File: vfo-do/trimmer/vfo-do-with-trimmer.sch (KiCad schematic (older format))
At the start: 19 parts, among them J1 Fréquence, J10 GPS, J2 Bande, J3 Reset, J4 Résolution, J5 Si5351, J8 LCD, J9 Alim +12V, U1 L7805

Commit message: plaque standard 10x5
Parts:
- added TP1, TP2, TP3, TP4: TestPoint_Alt, MountingHole:MountingHole_3.2mm_M3_Pad_Via, symbol Connector:TestPoint_Alt
- A1: symbol arduino_nano_v3_5v_input:Arduino_Nano_v3.x -> vfo-do-with-trimmer-rescue:Arduino_Nano_v3.x-arduino_nano_v3_5v_input
- U1: symbol arduino_nano_v3_5v_input:L7805 -> vfo-do-with-trimmer-rescue:L7805-arduino_nano_v3_5v_input
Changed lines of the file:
@@
 	8450 1000 8700 1000
 $Comp
-L arduino_nano_v3_5v_input:Arduino_Nano_v3.x A1
+L vfo-do-with-trimmer-rescue:Arduino_Nano_v3.x-arduino_nano_v3_5v_input A1
 U 1 1 5F40DF5B
 P 1950 2050
@@
 Connection ~ 7600 1000
 $Comp
-L arduino_nano_v3_5v_input:L7805 U1
+L vfo-do-with-trimmer-rescue:L7805-arduino_nano_v3_5v_input U1
 U 1 1 5F44051C
 P 8150 1000
@@
 Text Label 9350 3950 0    50   ~ 0
 K
+$Comp
+L Connector:TestPoint_Alt TP1
+U 1 1 5F44EF81
+P 4800 1700
+F 0 "TP1" H 4858 1818 50  0000 L CNN
+F 1 "TestPoint_Alt" H 4858 1727 50  0000 L CNN
+F 2 "MountingHole:MountingHole_3.2mm_M3_Pad_Via" H 5000 1700 50  0001 C CNN
+F 3 "~" H 5000 1700 50  0001 C CNN
+	1    4800 1700
+	1    0    0    -1
+$EndComp
+$Comp
+L Connector:TestPoint_Alt TP2
+U 1 1 5F44F871
+P 5100 1700
+F 0 "TP2" H 5158 1818 50  0000 L CNN
+F 1 "TestPoint_Alt" H 5158 1727 50  0000 L CNN
+F 2 "MountingHole:MountingHole_3.2mm_M3_Pad_Via" H 5300 1700 50  0001 C CNN
+F 3 "~" H 5300 1700 50  0001 C CNN
+	1    5100 1700
+	1    0    0    -1
+$EndComp
+$Comp
+L Connector:TestPoint_Alt TP3
+U 1 1 5F44FBE5
+P 5450 1700
+F 0 "TP3" H 5508 1818 50  0000 L CNN
+F 1 "TestPoint_Alt" H 5508 1727 50  0000 L CNN
+F 2 "MountingHole:MountingHole_3.2mm_M3_Pad_Via" H 5650 1700 50  0001 C CNN
+F 3 "~" H 5650 1700 50  0001 C CNN
+	1    5450 1700
+	1    0    0    -1
+$EndComp
+$Comp
+L Connector:TestPoint_Alt TP4
+U 1 1 5F44FF88
+P 5750 1700
+F 0 "TP4" H 5808 1818 50  0000 L CNN
+F 1 "TestPoint_Alt" H 5808 1727 50  0000 L CNN
+F 2 "MountingHole:MountingHole_3.2mm_M3_Pad_Via" H 5950 1700 50  0001 C CNN
+F 3 "~" H 5950 1700 50  0001 C CNN
+	1    5750 1700
+	1    0    0    -1
+$EndComp
+$Comp
+L power:GND #PWR0124
+U 1 1 5F4502D5
+P 4800 1700
+F 0 "#PWR0124" H 4800 1450 50  0001 C CNN
+F 1 "GND" H 4805 1527 50  0000 C CNN
+F 2 "" H 4800 1700 50  0001 C CNN
+F 3 "" H 4800 1700 50  0001 C CNN
+	1    4800 1700
+	1    0    0    -1
+$EndComp
+$Comp
+L power:GND #PWR0125
+U 1 1 5F450BEC
+P 5100 1700
+F 0 "#PWR0125" H 5100 1450 50  0001 C CNN
+F 1 "GND" H 5105 1527 50  0000 C CNN
+F 2 "" H 5100 1700 50  0001 C CNN
+F 3 "" H 5100 1700 50  0001 C CNN
+	1    5100 1700
+	1    0    0    -1
+$EndComp
+$Comp
+L power:GND #PWR0126
+U 1 1 5F451044
+P 5450 1700
+F 0 "#PWR0126" H 5450 1450 50  0001 C CNN
+F 1 "GND" H 5455 1527 50  0000 C CNN
+F 2 "" H 5450 1700 50  0001 C CNN
+F 3 "" H 5450 1700 50  0001 C CNN
+	1    5450 1700
+	1    0    0    -1
+$EndComp
+$Comp
+L power:GND #PWR0127
+U 1 1 5F451422
+P 5750 1700
+F 0 "#PWR0127" H 5750 1450 50  0001 C CNN
+F 1 "GND" H 5755 1527 50  0000 C CNN
+F 2 "" H 5750 1700 50  0001 C CNN
+F 3 "" H 5750 1700 50  0001 C CNN
+	1    5750 1700
+	1    0    0    -1
+$EndComp
 $EndSCHEMATC

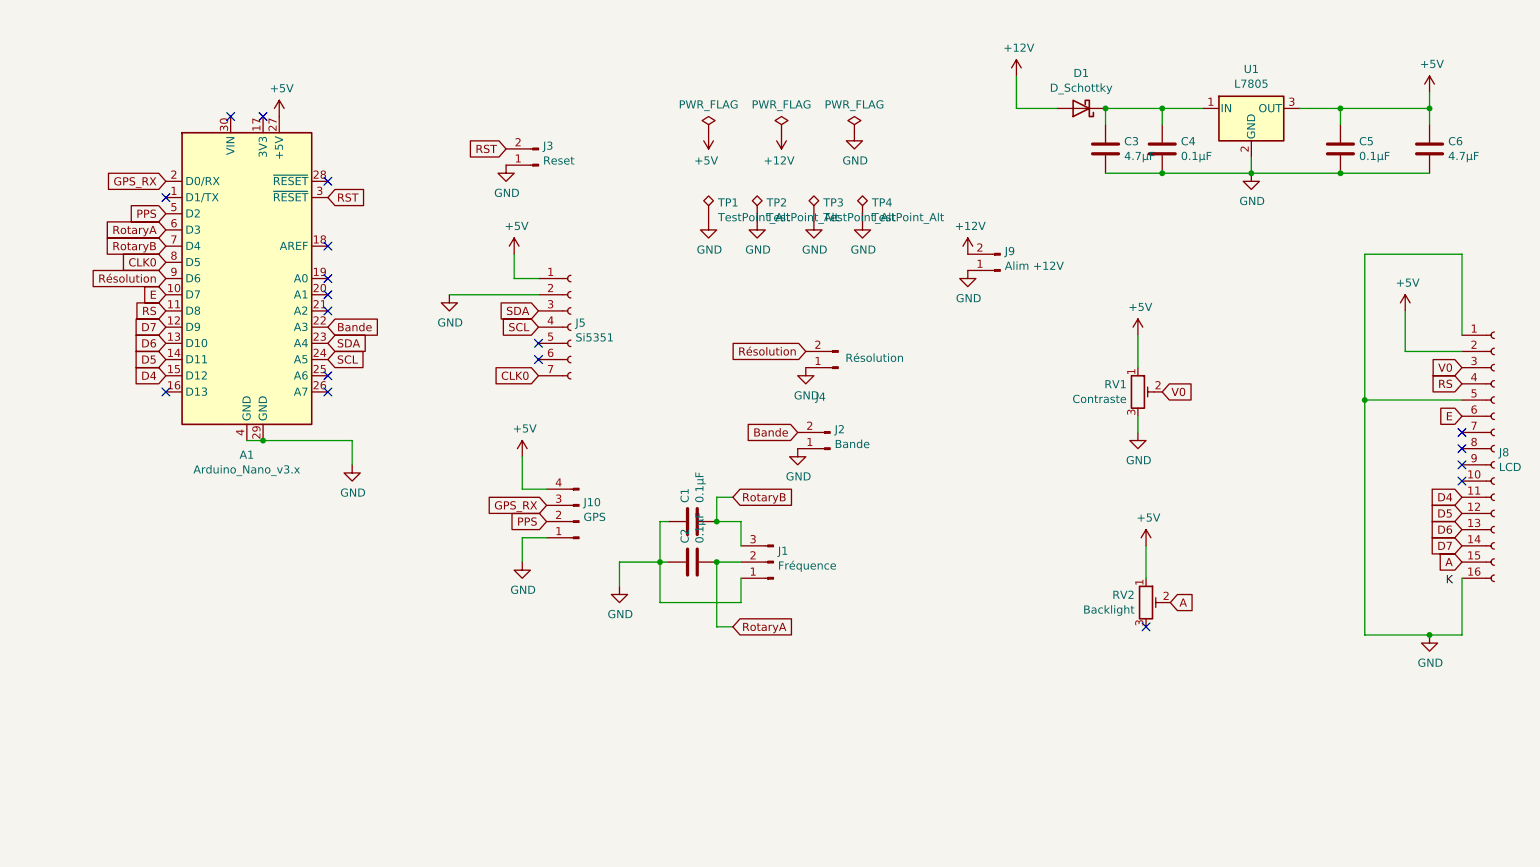
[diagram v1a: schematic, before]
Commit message: Ajout des bonnes empreintes pour les trimmers
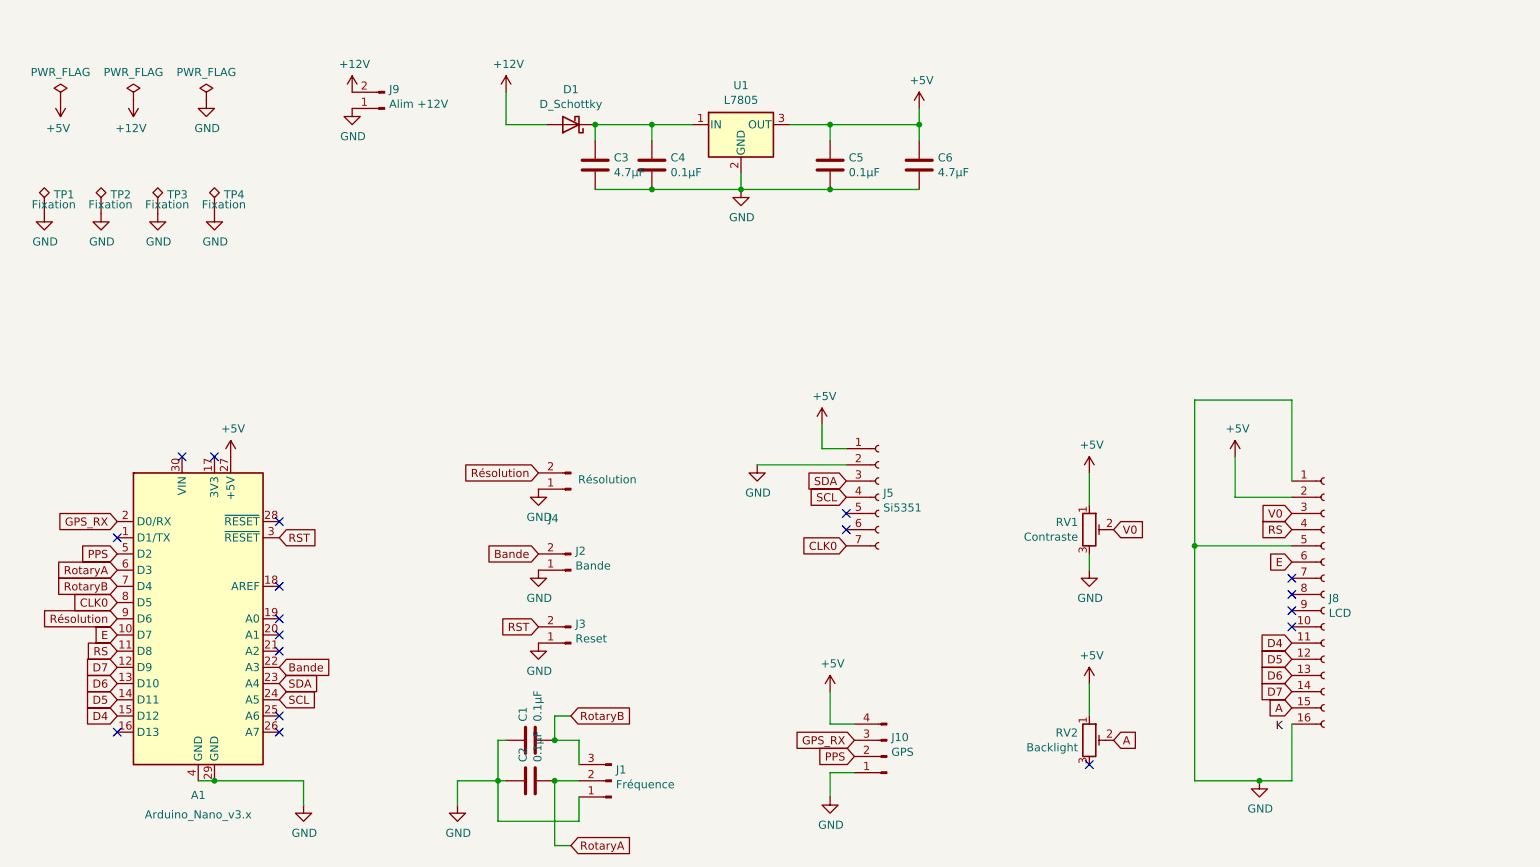
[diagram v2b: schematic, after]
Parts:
- RV1, RV2: footprint Potentiometer_SMD:Potentiometer_Vishay_TS53YL_Vertical -> rfa_trimmer:trimmer_3x3
- TP1, TP2, TP3, TP4: value TestPoint_Alt -> Fixation
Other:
- moved on the sheet: A1, C1, C2, C3, C4, C5, C6, D1, J1, J10, J2, J3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
